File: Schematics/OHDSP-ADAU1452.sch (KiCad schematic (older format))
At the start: 0 parts

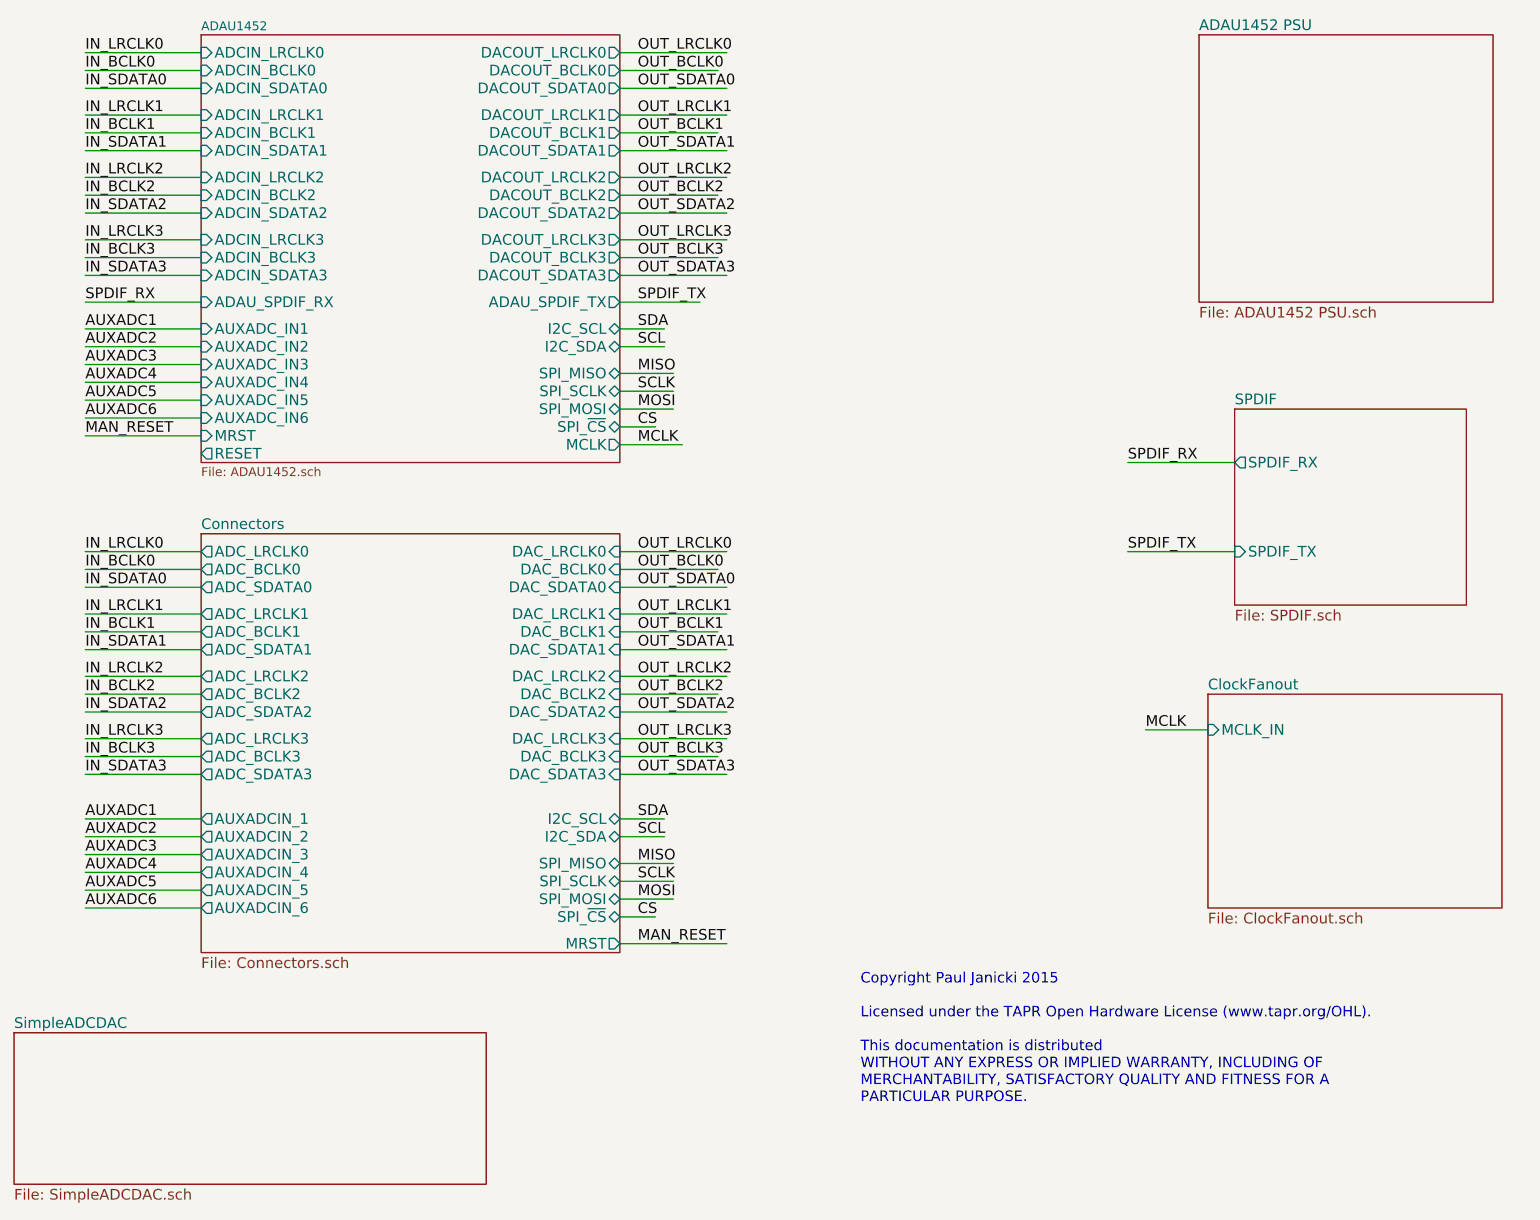
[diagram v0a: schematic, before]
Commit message: WIP
Removed Slave SPI as only really need I2C
Should free up some space on the board.
May look to change U.fl to SMA
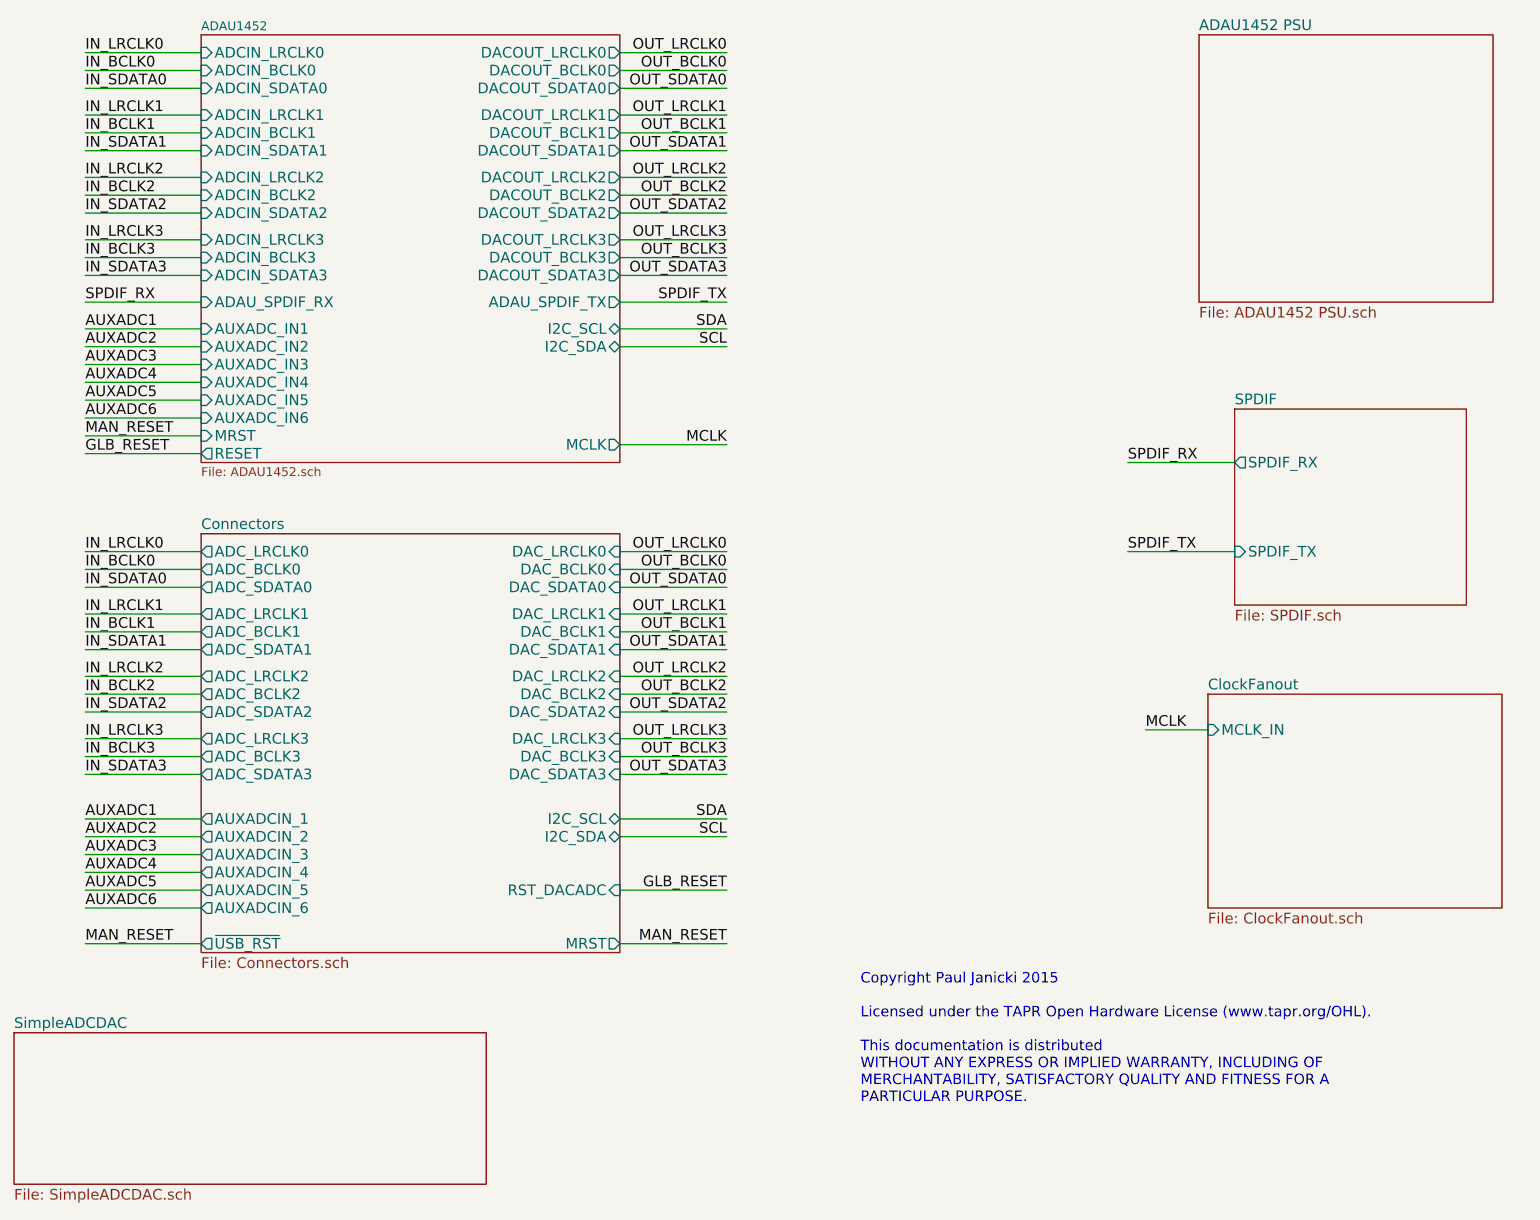
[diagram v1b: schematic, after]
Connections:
- net labels added: GLB_RESET
- net labels removed: CS, MISO, MOSI, SCLK
- wire segments 80 -> 75
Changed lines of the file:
@@
 F34 "I2C_SCL" B R 5650 2750 60
 F35 "I2C_SDA" B R 5650 2850 60
-F36 "SPI_MISO" B R 5650 3000 60
-F37 "SPI_SCLK" B R 5650 3100 60
-F38 "SPI_MOSI" B R 5650 3200 60
-F39 "SPI_~CS" B R 5650 3300 60
 F40 "MCLK" O R 5650 3400 60
 F41 "RESET" O L 3300 3450 60
@@
 Wire Wire Line
 	2650 2450 3300 2450
-Text Label 5750 1200 0    60   ~ 0
+Text Label 6250 1200 2    60   ~ 0
 OUT_LRCLK0
-Text Label 5750 1300 0    60   ~ 0
+Text Label 6250 1300 2    60   ~ 0
 OUT_BCLK0
-Text Label 5750 1400 0    60   ~ 0
+Text Label 6250 1400 2    60   ~ 0
 OUT_SDATA0
 Wire Wire Line
 	5650 1200 6250 1200
 Wire Wire Line
-	6200 1300 5650 1300
+	6250 1300 5650 1300
 Wire Wire Line
 	5650 1400 6250 1400
-Text Label 5750 1550 0    60   ~ 0
+Text Label 6250 1550 2    60   ~ 0
 OUT_LRCLK1
-Text Label 5750 1650 0    60   ~ 0
+Text Label 6250 1650 2    60   ~ 0
 OUT_BCLK1
-Text Label 5750 1750 0    60   ~ 0
+Text Label 6250 1750 2    60   ~ 0
 OUT_SDATA1
 Wire Wire Line
 	5650 1550 6250 1550
 Wire Wire Line
-	6200 1650 5650 1650
+	6250 1650 5650 1650
 Wire Wire Line
 	5650 1750 6250 1750
-Text Label 5750 1900 0    60   ~ 0
+Text Label 6250 1900 2    60   ~ 0
 OUT_LRCLK2
-Text Label 5750 2000 0    60   ~ 0
+Text Label 6250 2000 2    60   ~ 0
 OUT_BCLK2
-Text Label 5750 2100 0    60   ~ 0
+Text Label 6250 2100 2    60   ~ 0
 OUT_SDATA2
 Wire Wire Line
 	5650 1900 6250 1900
 Wire Wire Line
-	6200 2000 5650 2000
+	6250 2000 5650 2000
 Wire Wire Line
 	5650 2100 6250 2100
-Text Label 5750 2250 0    60   ~ 0
+Text Label 6250 2250 2    60   ~ 0
 OUT_LRCLK3
-Text Label 5750 2350 0    60   ~ 0
+Text Label 6250 2350 2    60   ~ 0
 OUT_BCLK3
-Text Label 5750 2450 0    60   ~ 0
+Text Label 6250 2450 2    60   ~ 0
 OUT_SDATA3
 Wire Wire Line
 	5650 2250 6250 2250
 Wire Wire Line
-	6200 2350 5650 2350
+	6250 2350 5650 2350
 Wire Wire Line
 	5650 2450 6250 2450
@@
 F14 "I2C_SCL" B R 5650 5500 60
 F15 "I2C_SDA" B R 5650 5600 60
-F16 "SPI_MISO" B R 5650 5750 60
-F17 "SPI_SCLK" B R 5650 5850 60
-F18 "SPI_MOSI" B R 5650 5950 60
-F19 "SPI_~CS" B R 5650 6050 60
-F20 "ADC_LRCLK1" O L 3300 4350 60
-F21 "ADC_BCLK1" O L 3300 4450 60
-F22 "ADC_SDATA1" O L 3300 4550 60
-F23 "ADC_LRCLK2" O L 3300 4700 60
-F24 "ADC_BCLK2" O L 3300 4800 60
-F25 "ADC_SDATA2" O L 3300 4900 60
-F26 "ADC_LRCLK3" O L 3300 5050 60
-F27 "ADC_BCLK3" O L 3300 5150 60
-F28 "ADC_SDATA3" O L 3300 5250 60
-F29 "DAC_LRCLK1" I R 5650 4350 60
-F30 "DAC_BCLK1" I R 5650 4450 60
-F31 "DAC_SDATA1" I R 5650 4550 60
-F32 "DAC_LRCLK2" I R 5650 4700 60
-F33 "DAC_BCLK2" I R 5650 4800 60
-F34 "DAC_SDATA2" I R 5650 4900 60
-F35 "DAC_LRCLK3" I R 5650 5050 60
-F36 "DAC_BCLK3" I R 5650 5150 60
-F37 "DAC_SDATA3" I R 5650 5250 60
-F38 "MRST" O R 5650 6200 60
+F16 "ADC_LRCLK1" O L 3300 4350 60
+F17 "ADC_BCLK1" O L 3300 4450 60
+F18 "ADC_SDATA1" O L 3300 4550 60
+F19 "ADC_LRCLK2" O L 3300 4700 60
+F20 "ADC_BCLK2" O L 3300 4800 60
+F21 "ADC_SDATA2" O L 3300 4900 60
+F22 "ADC_LRCLK3" O L 3300 5050 60
+F23 "ADC_BCLK3" O L 3300 5150 60
+F24 "ADC_SDATA3" O L 3300 5250 60
+F25 "DAC_LRCLK1" I R 5650 4350 60
+F26 "DAC_BCLK1" I R 5650 4450 60
+F27 "DAC_SDATA1" I R 5650 4550 60
+F28 "DAC_LRCLK2" I R 5650 4700 60
+F29 "DAC_BCLK2" I R 5650 4800 60
+F30 "DAC_SDATA2" I R 5650 4900 60
+F31 "DAC_LRCLK3" I R 5650 5050 60
+F32 "DAC_BCLK3" I R 5650 5150 60
+F33 "DAC_SDATA3" I R 5650 5250 60
+F34 "MRST" O R 5650 6200 60
+F35 "~USB_RST" O L 3300 6200 60
+F36 "RST_DACADC" I R 5650 5900 60
 $EndSheet
 Text Label 2650 4000 0    60   ~ 0
@@
 Wire Wire Line
 	2650 5250 3300 5250
-Text Label 5750 4000 0    60   ~ 0
+Text Label 6250 4000 2    60   ~ 0
 OUT_LRCLK0
-Text Label 5750 4100 0    60   ~ 0
+Text Label 6250 4100 2    60   ~ 0
 OUT_BCLK0
-Text Label 5750 4200 0    60   ~ 0
+Text Label 6250 4200 2    60   ~ 0
 OUT_SDATA0
 Wire Wire Line
 	5650 4000 6250 4000
 Wire Wire Line
-	6200 4100 5650 4100
+	6250 4100 5650 4100
 Wire Wire Line
 	5650 4200 6250 4200
-Text Label 5750 4350 0    60   ~ 0
+Text Label 6250 4350 2    60   ~ 0
 OUT_LRCLK1
-Text Label 5750 4450 0    60   ~ 0
+Text Label 6250 4450 2    60   ~ 0
 OUT_BCLK1
-Text Label 5750 4550 0    60   ~ 0
+Text Label 6250 4550 2    60   ~ 0
 OUT_SDATA1
 Wire Wire Line
 	5650 4350 6250 4350
 Wire Wire Line
-	6200 4450 5650 4450
+	6250 4450 5650 4450
 Wire Wire Line
 	5650 4550 6250 4550
-Text Label 5750 4700 0    60   ~ 0
+Text Label 6250 4700 2    60   ~ 0
 OUT_LRCLK2
-Text Label 5750 4800 0    60   ~ 0
+Text Label 6250 4800 2    60   ~ 0
 OUT_BCLK2
-Text Label 5750 4900 0    60   ~ 0
+Text Label 6250 4900 2    60   ~ 0
 OUT_SDATA2
 Wire Wire Line
 	5650 4700 6250 4700
 Wire Wire Line
-	6200 4800 5650 4800
+	6250 4800 5650 4800
 Wire Wire Line
 	5650 4900 6250 4900
-Text Label 5750 5050 0    60   ~ 0
+Text Label 6250 5050 2    60   ~ 0
 OUT_LRCLK3
-Text Label 5750 5150 0    60   ~ 0
+Text Label 6250 5150 2    60   ~ 0
 OUT_BCLK3
-Text Label 5750 5250 0    60   ~ 0
+Text Label 6250 5250 2    60   ~ 0
 OUT_SDATA3
 Wire Wire Line
 	5650 5050 6250 5050
 Wire Wire Line
-	6200 5150 5650 5150
+	6250 5150 5650 5150
 Wire Wire Line
 	5650 5250 6250 5250
-Text Label 5750 2600 0    60   ~ 0
+Text Label 6250 2600 2    60   ~ 0
 SPDIF_TX
 Text Label 2650 2600 0    60   ~ 0
@@
 	9100 3500 8500 3500
 Wire Wire Line
-	5650 2600 6100 2600
+	5650 2600 6250 2600
 Wire Wire Line
 	2650 2600 3300 2600
@@
 Wire Wire Line
 	3300 3250 2650 3250
-Text Label 5750 3400 0    60   ~ 0
+Text Label 6250 3400 2    60   ~ 0
 MCLK
 Wire Wire Line
-	5650 3400 6000 3400
+	5650 3400 6250 3400
 Text Label 8600 5000 0    60   ~ 0
 MCLK
 Wire Wire Line
 	8600 5000 8950 5000
-Text Label 5750 2750 0    60   ~ 0
+Text Label 6250 2750 2    60   ~ 0
 SDA
-Text Label 5750 2850 0    60   ~ 0
+Text Label 6250 2850 2    60   ~ 0
 SCL
-Text Label 5750 3000 0    60   ~ 0
-MISO
-Text Label 5750 3100 0    60   ~ 0
-SCLK
-Text Label 5750 3200 0    60   ~ 0
-MOSI
-Text Label 5750 3300 0    60   ~ 0
-CS
-Wire Wire Line
-	5650 2750 5900 2750
-Wire Wire Line
-	5650 2850 5900 2850
-Wire Wire Line
-	5650 3000 5950 3000
-Wire Wire Line
-	5650 3100 5950 3100
-Wire Wire Line
-	5650 3200 5950 3200
-Wire Wire Line
-	5650 3300 5850 3300
-Text Label 5750 5500 0    60   ~ 0
+Wire Wire Line
+	5650 2750 6250 2750
+Wire Wire Line
+	5650 2850 6250 2850
+Text Label 6250 5500 2    60   ~ 0
 SDA
-Text Label 5750 5600 0    60   ~ 0
+Text Label 6250 5600 2    60   ~ 0
 SCL
-Text Label 5750 5750 0    60   ~ 0
-MISO
-Text Label 5750 5850 0    60   ~ 0
-SCLK
-Text Label 5750 5950 0    60   ~ 0
-MOSI
-Text Label 5750 6050 0    60   ~ 0
-CS
-Wire Wire Line
-	5650 5500 5900 5500
-Wire Wire Line
-	5650 5600 5900 5600
-Wire Wire Line
-	5650 5750 5950 5750
-Wire Wire Line
-	5650 5850 5950 5850
-Wire Wire Line
-	5650 5950 5950 5950
-Wire Wire Line
-	5650 6050 5850 6050
+Wire Wire Line
+	5650 5500 6250 5500
+Wire Wire Line
+	5650 5600 6250 5600
 Text Label 2650 5800 0    60   ~ 0
 AUXADC4
@@
 Text Notes 7000 7100 0    59   ~ 0
 Copyright Paul Janicki 2015\n\nLicensed under the TAPR Open Hardware License (www.tapr.org/OHL).\n\nThis documentation is distributed\nWITHOUT ANY EXPRESS OR IMPLIED WARRANTY, INCLUDING OF\nMERCHANTABILITY, SATISFACTORY QUALITY AND FITNESS FOR A\nPARTICULAR PURPOSE.\n
-Text Label 5750 6200 0    60   ~ 0
+Text Label 6250 6200 2    60   ~ 0
 MAN_RESET
 Wire Wire Line
@@
 F1 "SimpleADCDAC.sch" 60
 $EndSheet
+Text Label 2650 6200 0    60   ~ 0
+MAN_RESET
+Wire Wire Line
+	2650 6200 3300 6200
+Text Label 2650 3450 0    60   ~ 0
+GLB_RESET
+Wire Wire Line
+	2650 3450 3300 3450
+Text Label 6250 5900 2    60   ~ 0
+GLB_RESET
+Wire Wire Line
+	6250 5900 5650 5900
 $EndSCHEMATC

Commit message: WIP
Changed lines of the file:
@@
 F34 "I2C_SCL" B R 5650 2750 60
 F35 "I2C_SDA" B R 5650 2850 60
-F40 "MCLK" O R 5650 3400 60
-F41 "RESET" O L 3300 3450 60
-F42 "MRST" I L 3300 3350 60
+F36 "MCLK" O R 5650 3400 60
+F37 "GLB_RESET" O L 3300 3450 60
+F38 "MAN_RST_IN" I L 3300 3350 60
 $EndSheet
 $Sheet
@@
 F32 "DAC_BCLK3" I R 5650 5150 60
 F33 "DAC_SDATA3" I R 5650 5250 60
-F34 "MRST" O R 5650 6200 60
+F34 "PI_RST_OUT" O R 5650 6200 60
 F35 "~USB_RST" O L 3300 6200 60
 F36 "RST_DACADC" I R 5650 5900 60

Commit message: WIP
Add master audio clock to I2S headers.
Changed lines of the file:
@@
 $Descr A4 11693 8268
 encoding utf-8
-Sheet 1 7
+Sheet 1 6
 Title ""
 Date "10 feb 2015"
@@
 $EndSheet
 $Sheet
-S 8950 4800 1650 1200
-U 54E20ECF
-F0 "ClockFanout" 60
-F1 "ClockFanout.sch" 60
-F2 "MCLK_IN" I L 8950 5000 60
-$EndSheet
-$Sheet
 S 9100 3200 1300 1100
 U 54E30917
@@
 F35 "~USB_RST" O L 3300 6200 60
 F36 "RST_DACADC" I R 5650 5900 60
+F37 "MCLK_IN" I R 5650 6050 60
 $EndSheet
 Text Label 2650 4000 0    60   ~ 0
@@
 Wire Wire Line
 	5650 3400 6250 3400
-Text Label 8600 5000 0    60   ~ 0
-MCLK
-Wire Wire Line
-	8600 5000 8950 5000
 Text Label 6250 2750 2    60   ~ 0
 SDA
@@
 Wire Wire Line
 	6250 5900 5650 5900
+Text Label 6250 6050 2    60   ~ 0
+MCLK
+Wire Wire Line
+	5650 6050 6250 6050
 $EndSCHEMATC
